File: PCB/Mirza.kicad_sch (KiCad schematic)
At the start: 99 parts, among them J1 In, J2 Out, J3 Power, Q1 PMP5201Y, Q13 2SC3324, Q14 2SA1312, Q15 2SA1312, Q16 2SA1312, Q17 2SC3324, Q18 2SC3324, Q2 PMP4201Y, Q21 2SA1312, Q22 2SC3324, Q23 2SC3324, Q24 2SA1312, Q25 D45H11, Q26 D44H11, Q3 2SA1312, Q4 2SC3324, Q5 2SC3324, Q6 2SC3324, Q7 2SA1312, Q8 2SA1312, U1 OPA604

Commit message: Initial public upload
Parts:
- removed R1, R6: 100k, Resistor_SMD:R_MiniMELF_MMA-0204, symbol Device:R_Small
- added H3, H4, H5, H6: JLC Tooling Hole, Ariamelon-HolePad:MountingHole_JLC-Tooling, symbol Mechanical:MountingHole
- added R1 (x4): 1, Resistor_SMD:R_MiniMELF_MMA-0204, symbol Device:R_Small
- added R6: 10k, Resistor_SMD:R_MiniMELF_MMA-0204, symbol Device:R_Small
- added R6: 1M, Resistor_SMD:R_MiniMELF_MMA-0204, symbol Device:R_Small
- C1, C2: value 1u -> 100n; LCSC (none) -> C85866; Manufacturer No. GRT21BR71H105KE01K -> GCM21BR72A104KA37L; Voltage (none) -> 100V
- C10, C6, C7: LCSC (none) -> C440149; Manufacturer No. 08052U470FAT2A -> GCM21A5C2E470JX01D; Voltage (none) -> 250V
- C101, C11, C12, C8, C9: LCSC (none) -> C437488; Manufacturer No. 08052U101FAT2A -> GCM21A7U2E101JX01D; Voltage (none) -> 250V
- C14, C15, C17, C18: footprint Capacitor_THT:CP_Radial_D6.3mm_P2.50mm -> Ariamelon-Device:CP_Radial_D6.3mm_P2.50mm; LCSC (none) -> C264049; Manufacturer No. EEU-FR1E151 -> EEUFR1E101; Voltage (none) -> 25V
- C3, C4: LCSC (none) -> C85866; Manufacturer No. GRT21BR71H104KE01L -> GCM21BR72A104KA37L; Voltage (none) -> 100V
- F1, F2: LCSC (none) -> C492011; Manufacturer No. 1206L050/24WR -> SMD1206P050TF/24
- H1, H2: footprint MountingHole:MountingHole_3.2mm_M3_Pad -> Ariamelon-HolePad:MountingHole_3.2mm_M3_Pad
- J1: now left out of the parts list
- Q1: value PMP5201Y -> BCM857BS; LCSC (none) -> C105887; Manufacturer No. PMP5201Y -> BCM857BS,115
- Q2: value PMP4201Y -> BCM847BS; LCSC (none) -> C396099; Manufacturer No. PMP4201Y -> BCM847BS,115
- Q2: value PMP4201Y -> BCM847BS; footprint Package_TO_SOT_SMD:SOT-363_SC-70-6 -> Ariamelon-Package:SOT-363_SC-70-6; LCSC (none) -> C396099; Manufacturer No. PMP4201Y -> BCM847BS,115
- Q25: Manufacturer No. (none) -> D45H11G
- Q26: Manufacturer No. (none) -> D44H11G
- R1: LCSC (none) -> C2074322; Manufacturer No. (none) -> MMA02040C1009FB300
- R1: LCSC (none) -> C2086951; Manufacturer No. (none) -> MMA02040C6809FB300
- R1, R5, R8: LCSC (none) -> C1884632; Manufacturer No. (none) -> MMA02040C5600FB300
- R1, R5: LCSC (none) -> C2074282; Manufacturer No. (none) -> MMA02040C2200FB300
- R1: LCSC (none) -> C2074241; Manufacturer No. (none) -> MMA02040C1500FB300
- R1: value 0R33 -> 1; footprint Resistor_SMD:R_MELF_MMB-0207 -> Resistor_SMD:R_MiniMELF_MMA-0204; LCSC (none) -> C2074959; Manufacturer No. (none) -> MMA02040C1008FB300
- R101, R6: LCSC (none) -> C1884620; Manufacturer No. (none) -> MMA02040C2201FB300
- R101, R6: value 100k -> 10k; LCSC (none) -> C2084764; Manufacturer No. (none) -> MMA02040C1002FB300
- R6: LCSC (none) -> C4339242; Manufacturer No. (none) -> MMA02040C1004FB300
- RV2, RV3: LCSC (none) -> C780233; Manufacturer No. (none) -> 3266W-1-102LF
- U1: value OPA604 -> ADA4522-1; LCSC (none) -> C160794; Manufacturer No. (none) -> ADA4522-1ARZ-R7
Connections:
- net +18V: now also F1.1, Q1.4 (E2), R101.2; no longer F1.2, Q1.1 (E1), R101.1
- net -18V: now also F2.1, Q2.4 (E2), R1.2, R101.2; no longer F2.2, Q2.1 (E1), R1.1, R101.1
- net Amp_FB: now also R1.1, R1.2, R1.2, R6.1; no longer R1.1, R1.1, R1.2
- net Amp_Out: now also R1.1, R1.1, R1.2, R6.2, R1.1, R1.1, R1.2, R1.2; no longer R1.1, R1.2, R1.2, R6.1
- net GND: now also C2.2, C4.1, C8.2, R1.1, R6.2; no longer C2.1, C4.2, C8.1, R1.2
- net VCC: now also Q2.4 (E2), R1.1, R5.2, R5.2; no longer Q2.1 (E1), R1.2, R5.1, R5.1
- net VEE: now also C4.2, Q1.4 (E2), R5.1, R8.1; no longer C4.1, Q1.1 (E1), R5.2, R8.2
- net at J3.1 (Pin_1): now also F1.2; no longer F1.1
- net at U1.6: now also C1.1, R6.2; no longer C1.2
- net at Q16.1 (B), R5.2: now also R6.1; no longer R6.2
- net at C11.1, Q23.1 (B), R1.2: now also Q1.6 (C1); no longer Q1.3 (C2)
- net at C101.2, R1.1: now also R101.2; no longer R101.1
- net at J1.2 (Pin_2): now also R101.1; no longer R101.2
- net at C9.1, R6.1: now also C7.2; no longer C7.1
- net at Q2.2 (B1): now also C14.1, R101.1; no longer Q2.4 (E2)
- net at C12.1, Q24.2 (C), Q26.1 (B): now also R1.1; no longer R1.2
- net at Q21.2 (C), Q24.3 (E), Q26.2 (C): now also R1.2, R1.2, R1.2; no longer R1.1
- net at Q17.1 (B), R5.1: now also R6.2; no longer R6.1
- net at Q1.2 (B1), Q1.4 (E2): now also R5.1; no longer R5.2
- net at Q1.5 (B2), Q1.6 (C1): now also R6.1; no longer R6.2
- net at Q2.1 (E1), Q2.3 (C2): now also Q2.2 (B1), Q2.5 (B2)
- net at Q2.4 (E2): now also R1.2; no longer R5.1
- net at Q2.4 (E2), Q2.6 (C1): no longer Q2.2 (B1), Q2.5 (B2)
- net at C12.2, Q24.1 (B): now also Q2.6 (C1), R1.2; no longer Q2.3 (C2), R1.1
- net at Q14.2 (C), Q18.3 (E): now also Q2.6 (C1); no longer Q2.3 (C2)
- net at R5.1: now also Q1.1 (E1), Q1.5 (B2); no longer RV2.3
- net at Q1.2 (B1): now also C14.2, R101.1; no longer Q1.4 (E2)
- net at U1.2 (-): now also C1.2, R6.1; no longer C1.1
- net at Q13.2 (C), Q15.3 (E): now also Q1.6 (C1); no longer Q1.3 (C2)
- net at Q1.2 (B1), Q1.5 (B2), Q1.6 (C1): now also Q1.1 (E1); no longer Q1.4 (E2)
- net at C6.1, Q1.2 (B1), Q1.5 (B2)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: now also Q1.3 (C2); no longer Q1.6 (C1)
- net at Q22.2 (C), Q23.3 (E), Q25.2 (C): now also R1.1, R1.1, R1.1; no longer R1.2
- net at Q22.3 (E): now also R1.1; no longer R1.2
- net at Q3.2 (C), Q7.3 (E): now also R1.2; no longer R1.1
- net at J3.4 (Pin_4): now also F2.2; no longer F2.1
- net at Q2.1 (E1): now also R5.2; no longer R1.2
- net at Q2.2 (B1), Q2.4 (E2): now also R8.2; no longer R8.1
- net at Q14.1 (B), Q2.2 (B1), Q2.5 (B2)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: now also C7.1, Q2.3 (C2); no longer C7.2, Q2.6 (C1)
- net at Q4.2 (C), Q6.3 (E): now also R1.1; no longer R1.2
- net at R1.2: now also Q7.1 (B), R1.1; no longer Q4.3 (E)
- net at Q2.3 (C2), Q8.1 (B): now also R1.2; no longer R1.1
- net at Q1.1 (E1): now also R1.2; no longer R1.1
- net at C6.2, C8.1: now also R6.1; no longer R6.2
- net at Q1.3 (C2): now also Q1.4 (E2); no longer Q1.1 (E1)
- net at Q1.4 (E2): now also R5.1; no longer R5.2
- net at Q2.5 (B2), Q2.6 (C1): now also R6.2; no longer R6.1
- net at R6.1, U1.3 (+): now also C2.1; no longer C2.2
- new net: Q1.2 (B1), Q1.3 (C2), R6.1
- new net: Q2.1 (E1), Q2.5 (B2)
- new net: Q2.2 (B1), Q2.3 (C2), R6.2
- new net: Q2.1 (E1), Q2.5 (B2), R5.1
- new net: R5.2, RV2.3
- new net: Q1.1 (E1), Q1.5 (B2)
- new net: C8.1, R1.2
- new net: Q4.3 (E), R1.1
- no-connect marks 2 -> 0
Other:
- note removed: "PGFB threshold = +14V"
- company: (none) -> Created by Ariamelon (https://github.com/Ariamelon/Mirza/)
- title: (none) -> Mirza Current-Feedback Amplifier Module
- moved on the sheet: A1, C10, C14, C15, C17, C18, C3, C4, C8, C9, F1, F2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

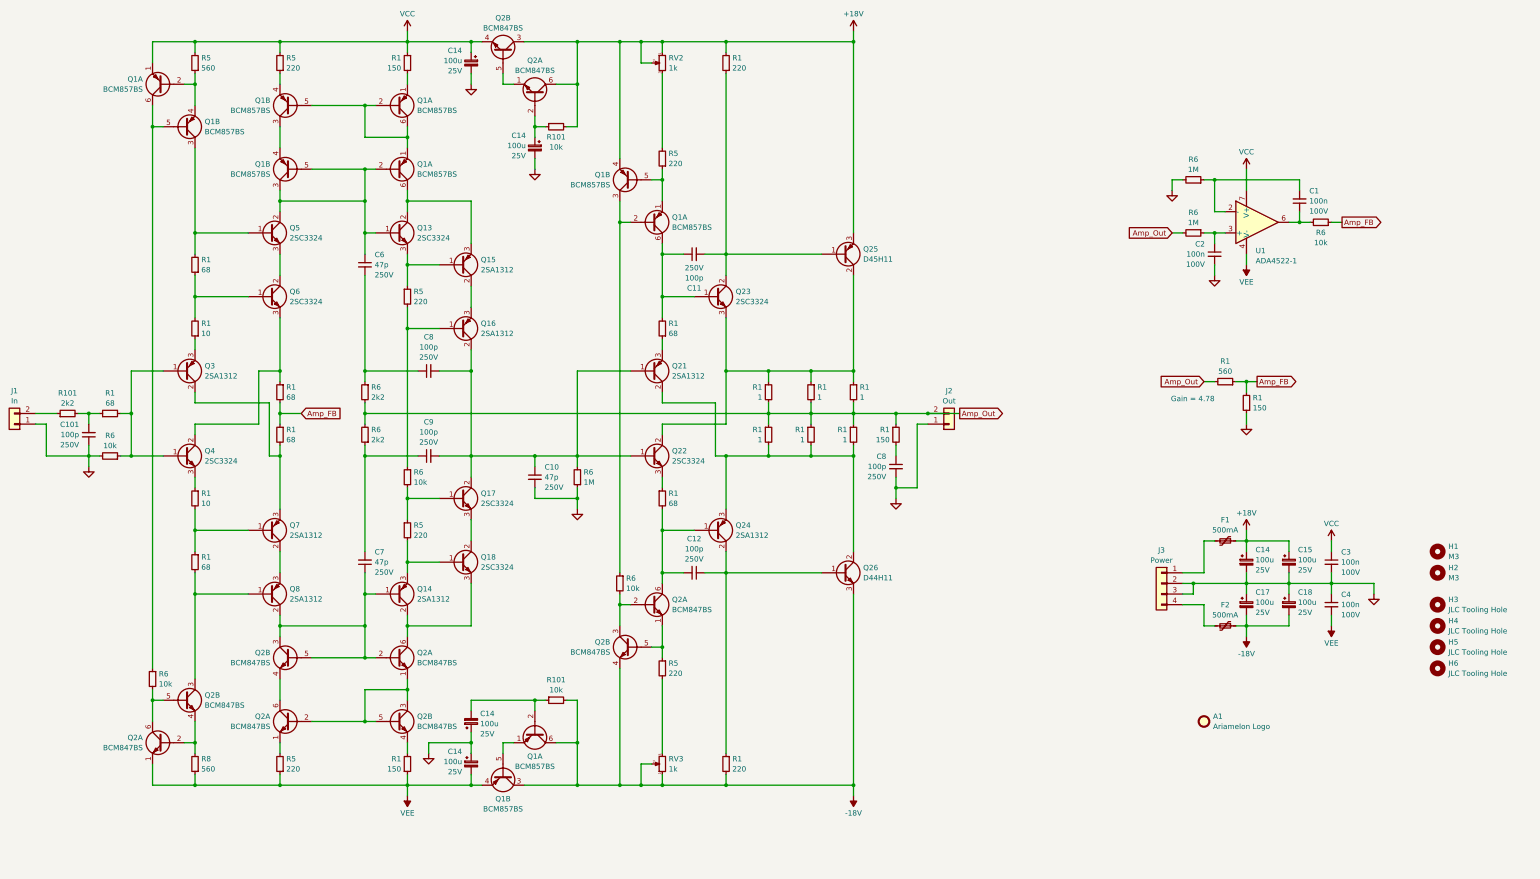
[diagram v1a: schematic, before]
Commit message: 17/09/2023 update
Repositioning of parts. Added interactive BOM. Changed some values. Removed PTC fuses. Lengthened board to add JST XH connectors.
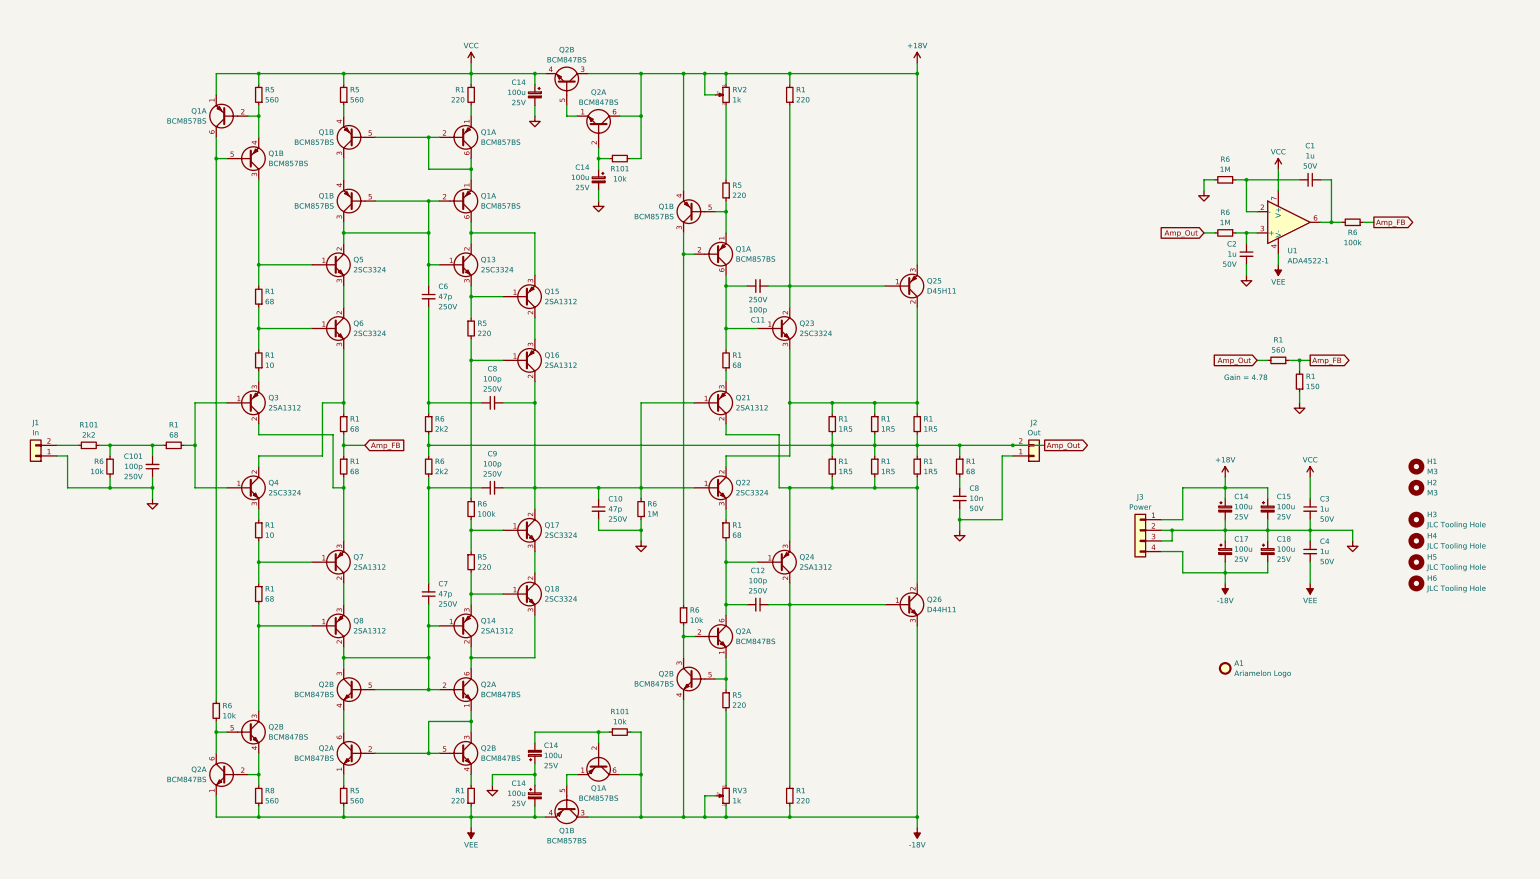
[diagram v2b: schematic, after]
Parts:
- removed F1, F2: 500mA, Ariamelon-Device:Fuse_1206_3216Metric, symbol Device:Polyfuse_Small
- removed R1 (x2): 1, Resistor_SMD:R_MiniMELF_MMA-0204, symbol Device:R_Small
- added R1 (x2): 1R5, Resistor_SMD:R_MiniMELF_MMA-0204, symbol Device:R_Small
- C1, C2, C3, C4: value 100n -> 1u; LCSC C85866 -> C126592; Manufacturer No. GCM21BR72A104KA37L -> GCM21BR71H105KA03L; Voltage 100V -> 50V
- C8: value 100p -> 10n; LCSC C437488 -> C161250; Manufacturer No. GCM21A7U2E101JX01D -> GCM2195C1H103JA16D; Voltage 250V -> 50V
- J1, J2: footprint Connector_PinHeader_2.54mm:PinHeader_1x02_P2.54mm_Vertical -> Connector_JST:JST_XH_B2B-XH-A_1x02_P2.50mm_Vertical
- J3: footprint Ariamelon-Header:PinHeader_1x04_P2.54mm_Vertical_MiddleGND -> Ariamelon-Connector:JST_XH_B4B-XH-A_1x04_P2.50mm_Vertical_MiddleGND
- R1: value 150 -> 220; LCSC C2074241 -> C2074282; Manufacturer No. MMA02040C1500FB300 -> MMA02040C2200FB300
- R1: value 1 -> 1R5; LCSC C2074959 -> C3008833; Manufacturer No. MMA02040C1008FB300 -> MMA02040C1508FB300
- R1: value 150 -> 68; LCSC C2074241 -> C2086951; Manufacturer No. MMA02040C1500FB300 -> MMA02040C6809FB300
- R5: value 220 -> 560; LCSC C2074282 -> C1884632; Manufacturer No. MMA02040C2200FB300 -> MMA02040C5600FB300
- R6: value 10k -> 100k; LCSC C2084764 -> C2836210; Manufacturer No. MMA02040C1002FB300 -> MMA02040C1003FB300
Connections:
- net +18V: now also J3.1 (Pin_1)
- net -18V: now also J3.4 (Pin_4)
- net Amp_Out: now also R1.1, R1.2
- net at Q3.1 (B), Q4.1 (B), R1.2: no longer R6.1
- net at C101.2, R1.1, R101.2: now also R6.1
- net at Q21.2 (C), Q24.3 (E), Q26.2 (C)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: now also R1.2
- net at Q22.2 (C), Q23.3 (E), Q25.2 (C)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: now also R1.1
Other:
- moved on the sheet: A1, C1, C10, C101, C11, C12, C14, C15, C17, C18, C2, C3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

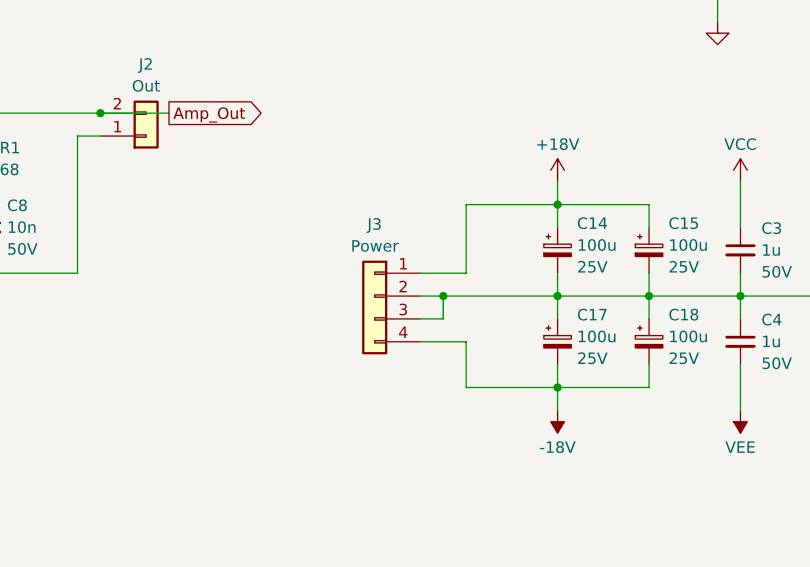
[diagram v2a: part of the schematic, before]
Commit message: 18/09/2023 update
Changed power header to JST XH 6-pin.
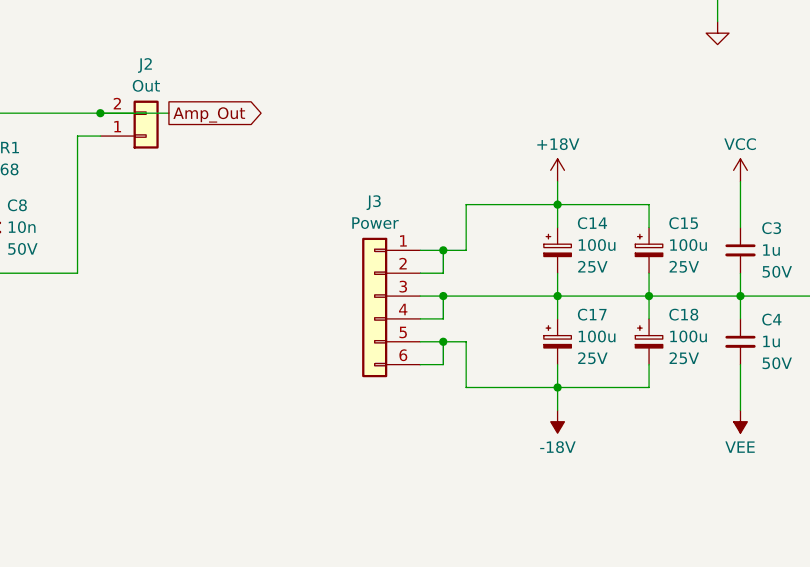
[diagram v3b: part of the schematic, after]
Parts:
- removed J3: Power, Ariamelon-Connector:JST_XH_B4B-XH-A_1x04_P2.50mm_Vertical_MiddleGND, symbol Connector_Generic:Conn_01x04
- added J3: Power, Ariamelon-Connector:JST_XH_B6B-XH-A_1x06_P2.50mm_Vertical_MiddleGND, symbol Connector_Generic:Conn_01x06
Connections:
- net +18V: now also J3.1 (Pin_1), J3.2 (Pin_2)
- net -18V: now also J3.5 (Pin_5), J3.6 (Pin_6)
- net GND: now also J3.3 (Pin_3), J3.4 (Pin_4)
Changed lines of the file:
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@@
   (title_block
     (title "Mirza Current-Feedback Amplifier Module")
-    (date "2023-09-17")
+    (date "2023-09-18")
     (rev "V1.0")
     (company "Created by Ariamelon (https://github.com/Ariamelon/Mirza/)")
@@
   (junction (at 109.22 60.96) (diameter 0) (color 0 0 0 0)
   )
+  (junction (at 307.34 165.1) (diameter 0) (color 0 0 0 0)
+  )
   (junction (at 246.38 60.96) (diameter 0) (color 0 0 0 0)
   )
@@
   (junction (at 129.54 91.44) (diameter 0) (color 0 0 0 0)
   )
+  (junction (at 307.34 175.26) (diameter 0) (color 0 0 0 0)
+  )
   (junction (at 200.66 111.76) (diameter 0) (color 0 0 0 0)
   )
@@
     (stroke (width 0) (type default))
   )
+  (wire (pts (xy 307.34 175.26) (xy 309.88 175.26))
+    (stroke (width 0) (type default))
+  )
   (wire (pts (xy 109.22 157.48) (xy 109.22 160.02))
     (stroke (width 0) (type default))
@@
     (stroke (width 0) (type default))
   )
+  (wire (pts (xy 307.34 165.1) (xy 304.8 165.1))
+    (stroke (width 0) (type default))
+  )
   (wire (pts (xy 307.34 172.72) (xy 307.34 170.18))
     (stroke (width 0) (type default))
@@
     (stroke (width 0) (type default))
   )
+  (wire (pts (xy 307.34 165.1) (xy 307.34 167.64))
+    (stroke (width 0) (type default))
+  )
   (wire (pts (xy 337.82 137.16) (xy 337.82 139.7))
     (stroke (width 0) (type default))
@@
     (stroke (width 0) (type default))
   )
+  (wire (pts (xy 307.34 165.1) (xy 309.88 165.1))
+    (stroke (width 0) (type default))
+  )
   (wire (pts (xy 129.54 223.52) (xy 132.08 223.52))
     (stroke (width 0) (type default))
@@
     (stroke (width 0) (type default))
   )
+  (wire (pts (xy 307.34 177.8) (xy 304.8 177.8))
+    (stroke (width 0) (type default))
+  )
   (wire (pts (xy 180.34 162.56) (xy 180.34 160.02))
     (stroke (width 0) (type default))
@@
     (stroke (width 0) (type default))
   )
-  (wire (pts (xy 304.8 167.64) (xy 309.88 167.64))
-    (stroke (width 0) (type default))
-  )
   (wire (pts (xy 129.54 91.44) (xy 132.08 91.44))
     (stroke (width 0) (type default))
@@
     (stroke (width 0) (type default))
   )
-  (wire (pts (xy 309.88 167.64) (xy 309.88 160.02))
+  (wire (pts (xy 309.88 165.1) (xy 309.88 160.02))
     (stroke (width 0) (type default))
   )
@@
     (stroke (width 0) (type default))
   )
+  (wire (pts (xy 307.34 175.26) (xy 307.34 177.8))
+    (stroke (width 0) (type default))
+  )
   (wire (pts (xy 200.66 111.76) (xy 205.74 111.76))
     (stroke (width 0) (type default))
@@
     (stroke (width 0) (type default))
   )
-  (wire (pts (xy 304.8 175.26) (xy 309.88 175.26))
+  (wire (pts (xy 304.8 175.26) (xy 307.34 175.26))
     (stroke (width 0) (type default))
   )
@@
     (stroke (width 0) (type default))
   )
+  (wire (pts (xy 307.34 167.64) (xy 304.8 167.64))
+    (stroke (width 0) (type default))
+  )
   (wire (pts (xy 139.7 68.58) (xy 139.7 71.12))
     (stroke (width 0) (type default))
@@
     )
   )
-  (symbol (lib_id "Connector_Generic:Conn_01x04") (at 299.72 170.18 0) (mirror y) (unit 1)
-    (in_bom no) (on_board yes) (dnp no) (fields_autoplaced)
-    (property "Reference" "J3" (at 299.72 162.2257 0)
-      (effects (font (size 1.27 1.27)))
-    )
-    (property "Value" "Power" (at 299.72 164.6499 0)
-      (effects (font (size 1.27 1.27)))
-    )
-    (property "Footprint" "Ariamelon-Connector:JST_XH_B4B-XH-A_1x04_P2.50mm_Vertical_MiddleGND" (at 299.72 170.18 0)
-      (effects (font (size 1.27 1.27)) hide)
-    )
-    (property "Datasheet" "~" (at 299.72 170.18 0)
-      (effects (font (size 1.27 1.27)) hide)
-    )
-    (property "LCSC" "" (at 299.72 170.18 0)
-      (effects (font (size 1.27 1.27)) hide)
-    )
-    (property "Voltage" "" (at 299.72 170.18 0)
-      (effects (font (size 1.27 1.27)) hide)
-    )
-    (pin "1")
-    (pin "2")
-    (pin "3")
-    (pin "4")
-    (instances
-      (project "Mirza"
-        (path "/fe9fc43f-1188-4d03-8e81-9a6232eb6dc0"
-          (reference "J3") (unit 1)
-        )
-      )
-    )
-  )
   (symbol (lib_id "Device:R_Small") (at 109.22 154.94 0) (mirror y) (unit 1)
     (in_bom yes) (on_board yes) (dnp no) (fields_autoplaced)
@@
         )
       )
+    )
+  )
+  (symbol (lib_id "Connector_Generic:Conn_01x06") (at 299.72 170.18 0) (mirror y) (unit 1)
+    (in_bom yes) (on_board yes) (dnp no) (fields_autoplaced)
+    (property "Reference" "J3" (at 299.72 159.6857 0)
+      (effects (font (size 1.27 1.27)))
+    )
+    (property "Value" "Power" (at 299.72 162.1099 0)
+      (effects (font (size 1.27 1.27)))
+    )
+    (property "Footprint" "Ariamelon-Connector:JST_XH_B6B-XH-A_1x06_P2.50mm_Vertical_MiddleGND" (at 299.72 170.18 0)
+      (effects (font (size 1.27 1.27)) hide)
+    )
+    (property "Datasheet" "~" (at 299.72 170.18 0)
+      (effects (font (size 1.27 1.27)) hide)
+    )
+    (pin "1")
+    (pin "2")
+    (pin "3")
+    (pin "4")
+    (pin "5")
+    (pin "6")
+    (instances
+      (project "Mirza"
+        (path "/fe9fc43f-1188-4d03-8e81-9a6232eb6dc0"
+          (reference "J3") (unit 1)
+        )
+      )
